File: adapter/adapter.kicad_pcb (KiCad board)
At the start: 2 copper layers, 93.6 x 71.8 mm, 44 parts, among them J10 Ribbon, J11 Ribbon, J12 Ribbon, J13 serial, J14 serial, J3 battery charge, J6 battery charge, J7 trackball, J8 trackball, J9 Ribbon, SW1 SW_SPST, SW2 SW_SPST, SW3 SW_SPDT, SW4 SW_SPDT, U1 eliteC, U2 eliteC

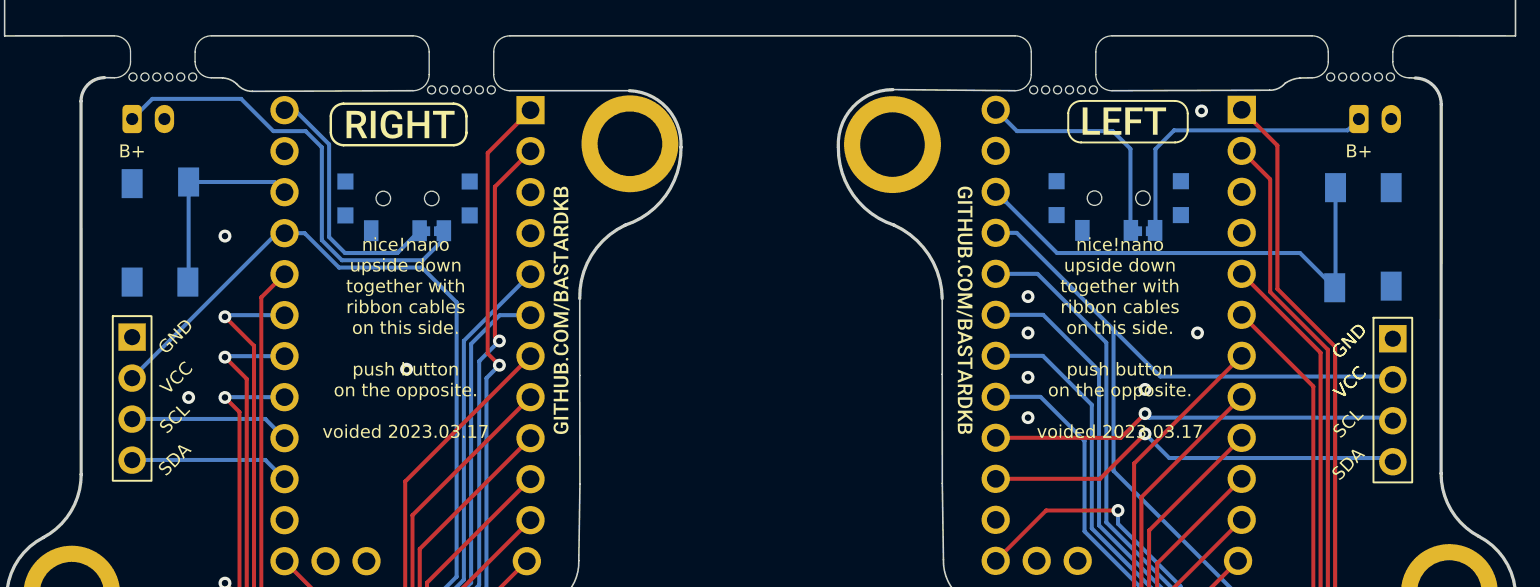
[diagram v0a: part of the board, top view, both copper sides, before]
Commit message: v0.2
removed serial ports
moved reset to be reachable
replace on/off switch to top and swapped to vertical through hole
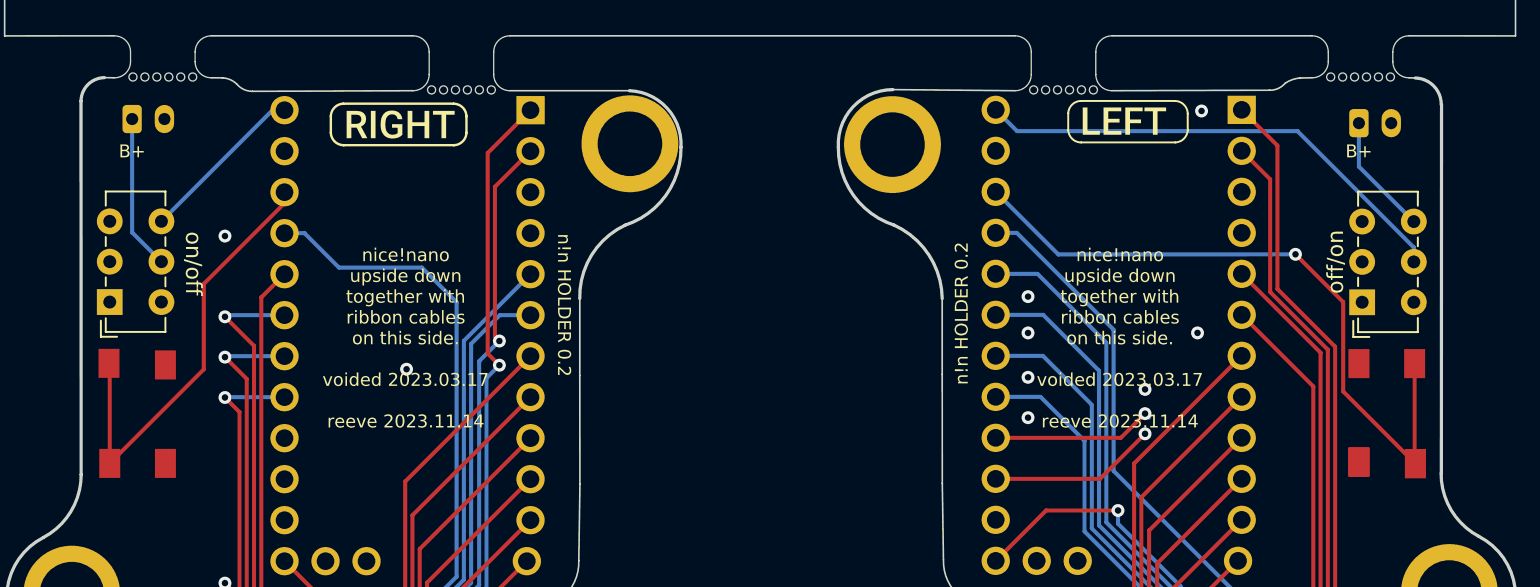
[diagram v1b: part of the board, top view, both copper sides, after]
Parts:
- removed J13, J14: serial, Library:PinHeader_1x04_P2.54mm_Vertical
- removed JP1, JP2: Jumper_2_Open, Library:power_switch_jumper
- removed SW3, SW4: SW_SPDT, Library:SW_SPDT+H-MSK12C01_hor(7pin_SMD)
- removed kibuzzard-61F01A92 (x2): G***, kibuzzard-61F01A92
- removed the kibuzzard-620B8593 at (133.5, 78.6)
- added ?: , , F.Cu at (196.0, 91.1)
- added ?: , , F.Cu at (192.5, 91.0)
- added REF**: SW3, Button_Switch_THT:SW_E-Switch_EG1271_SPDT, F.Cu at (115.1, 81.1)
- added off/on: SW_E-Switch_EG1271_SPDT, Button_Switch_THT:SW_E-Switch_EG1271_SPDT, F.Cu at (192.7, 81.1)
- SW1, SW2: moved to F.Cu
- moved SW1 11.3 mm to (116.9, 88.0)
- moved SW2 11.0 mm to (194.2, 88.0)
- moved J6 0.25 mm to (192.5, 70.0)
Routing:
- net +5V: track 115.5 -> 83.7 mm
- net bat_sw_l: track 28.4 -> 9.59 mm
- net sda_r: track 26.5 -> 10.4 mm
- net bat_r: track 14.4 -> 30.3 mm
- net scl_r: track 25.4 -> 10.2 mm
- net Rst: track 12.4 -> 27.6 mm
- net Rst2: track 29.7 -> 42.9 mm, vias 0 -> 1
- net bat_sw_r: track 18.4 -> 7.50 mm
- net scl_l: track 9.94 -> 0.00 mm
- net sda_l: track 9.94 -> 0.00 mm
- net bat_l: track 16.0 -> 11.1 mm
- net GND: vias 11 -> 10
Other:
- outline, holes or cut-outs redrawn
- board text added: "n!n HOLDER 0.2"
- board text added: "nice!nano upside down together with ribbon cables on this side. voided 2023.03.17 reeve 2023.11.14"
- board text added: "on/off"
- board text removed: "SCL"
- board text removed: "SDA"
- board text removed: "n!n HOLDER 0.1"
- board text removed: "nice!nano upside down together with ribbon cables on this side. push button on the opposite. voided 2023.03.17"

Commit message: Small fixes
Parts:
- removed kibuzzard-620B8593: G***, kibuzzard-620B8593
- moved J6 0.33 mm to (192.2, 70.0)
- moved J3 0.22 mm to (116.7, 69.8)
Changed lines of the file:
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@@
   )
   (footprint "Connector_JST:JST_PH_B2B-PH-K_1x02_P2.00mm_Vertical" (layer "F.Cu")
-    (at 192.5 70.004)
+    (at 192.175 70.002)
     (descr "JST PH series connector, B2B-PH-K (http://www.jst-mfg.com/product/pdf/eng/ePH.pdf), generated with kicad-footprint-generator")
     (tags "connector JST PH side entry")
@@
   )
   (footprint "Connector_JST:JST_PH_B2B-PH-K_1x02_P2.00mm_Vertical" (layer "F.Cu")
-    (at 116.5 69.75)
+    (at 116.725 69.75)
     (descr "JST PH series connector, B2B-PH-K (http://www.jst-mfg.com/product/pdf/eng/ePH.pdf), generated with kicad-footprint-generator")
     (tags "connector JST PH side entry")
@@
     )
   )
-  (footprint "kibuzzard-620B8593" (layer "B.Cu")
-    (at 177.5 78.6 180)
-    (descr "Converted using: scripting")
-    (tags "svg2mod")
-    (attr board_only exclude_from_pos_files exclude_from_bom)
-    (fp_text reference "kibuzzard-620B8593" (at 0 0.496912) (layer "B.SilkS") hide
-        (effects (font (size 0.000254 0.000254) (thickness 0.000003)) (justify mirror))
-    )
-    (fp_text value "G***" (at 0 -0.496912) (layer "B.SilkS") hide
-        (effects (font (size 0.000254 0.000254) (thickness 0.000003)) (justify mirror))
-    )
-    (fp_poly
-      (pts
-        (xy -0.393774 -0.496404)
-        (xy -0.512217 -0.496404)
-        (xy -0.15689 0.484001)
-        (xy -0.038447 0.484001)
-        (xy -0.393774 -0.496404)
-      )
-      (stroke (width 0) (type solid)) (fill solid) (layer "B.SilkS"))
-    (fp_poly
-      (pts
-        (xy -0.607095 -0.418889)
-        (xy -0.763984 -0.418889)
-        (xy -1.16644 0.221692)
-        (xy -1.16644 -0.418889)
-        (xy -1.32333 -0.418889)
-        (xy -1.32333 0.484001)
-        (xy -1.16644 0.484001)
-        (xy -0.762744 -0.15906)
-        (xy -0.762744 0.484001)
-        (xy -0.607095 0.484001)
-        (xy -0.607095 -0.418889)
-      )
-      (stroke (width 0) (type solid)) (fill solid) (layer "B.SilkS"))
-    (fp_poly
-      (pts
-        (xy 1.477739 -0.036277)
-        (xy 1.114351 -0.036277)
-        (xy 1.114351 -0.418889)
-        (xy 0.957461 -0.418889)
-        (xy 0.957461 0.484001)
-        (xy 1.531069 0.484001)
-        (xy 1.531069 0.357498)
-        (xy 1.114351 0.357498)
-        (xy 1.114351 0.088987)
-        (xy 1.477739 0.088987)
-        (xy 1.477739 -0.036277)
-      )
-      (stroke (width 0) (type solid)) (fill solid) (layer "B.SilkS"))
-    (fp_poly
-      (pts
-        (xy 2.175371 -0.036277)
-        (xy 1.811982 -0.036277)
-        (xy 1.811982 -0.418889)
-        (xy 1.655093 -0.418889)
-        (xy 1.655093 0.484001)
-        (xy 2.228701 0.484001)
-        (xy 2.228701 0.357498)
-        (xy 1.811982 0.357498)
-        (xy 1.811982 0.088987)
-        (xy 2.175371 0.088987)
-        (xy 2.175371 -0.036277)
-      )
-      (stroke (width 0) (type solid)) (fill solid) (layer "B.SilkS"))
-    (fp_poly
-      (pts
-        (xy -1.4796 0.008992)
-        (xy -1.636489 0.056121)
-        (xy -1.642794 0.14838)
-        (xy -1.661707 0.225068)
-        (xy -1.69323 0.286184)
-        (xy -1.76183 0.34618)
-        (xy -1.85415 0.366179)
-        (xy -1.944765 0.346258)
-        (xy -2.01321 0.286494)
-        (xy -2.045215 0.226033)
-        (xy -2.064749 0.150895)
-        (xy -2.071812 0.061082)
-        (xy -2.071812 0.008992)
-        (xy -2.065369 -0.082717)
-        (xy -2.046042 -0.159405)
-        (xy -2.013831 -0.221072)
-        (xy -1.94461 -0.281998)
-        (xy -1.85291 -0.302307)
-        (xy -1.760745 -0.282463)
-        (xy -1.69261 -0.222932)
-        (xy -1.661432 -0.161885)
-        (xy -1.642725 -0.084577)
-        (xy -1.636489 0.008992)
-        (xy -1.636489 0.056121)
-        (xy -1.4796 0.008992)
-        (xy -1.484698 -0.075861)
-        (xy -1.499995 -0.153479)
-        (xy -1.525488 -0.223862)
-        (xy -1.581221 -0.312384)
-        (xy -1.656643 -0.377651)
-        (xy -1.716347 -0.407451)
-        (xy -1.781769 -0.425331)
-        (xy -1.85291 -0.431292)
-        (xy -1.956702 -0.417881)
-        (xy -2.048557 -0.377651)
-        (xy -2.124677 -0.312617)
-        (xy -2.181262 -0.224792)
-        (xy -2.207342 -0.15527)
-        (xy -2.223155 -0.078996)
-        (xy -2.228701 0.004031)
-        (xy -2.228701 0.05488)
-        (xy -2.223499 0.139492)
-        (xy -2.207893 0.217213)
-        (xy -2.181882 0.288044)
-        (xy -2.146398 0.35016)
-        (xy -2.10237 0.401733)
-        (xy -2.049797 0.442764)
-        (xy -1.958253 0.482994)
-        (xy -1.85415 0.496404)
-        (xy -1.750048 0.483149)
-        (xy -1.658503 0.443384)
-        (xy -1.582927 0.378737)
-        (xy -1.526729 0.290835)
-        (xy -1.500821 0.220865)
-        (xy -1.485112 0.14366)
-        (xy -1.4796 0.059221)
-        (xy -1.4796 0.008992)
-      )
-      (stroke (width 0) (type solid)) (fill solid) (layer "B.SilkS"))
-    (fp_poly
-      (pts
-        (xy 0.801191 0.008992)
-        (xy 0.644302 0.056121)
-        (xy 0.637997 0.14838)
-        (xy 0.619084 0.225068)
-        (xy 0.587561 0.286184)
-        (xy 0.518961 0.34618)
-        (xy 0.426641 0.366179)
-        (xy 0.336026 0.346258)
-        (xy 0.267581 0.286494)
-        (xy 0.235576 0.226033)
-        (xy 0.216042 0.150895)
-        (xy 0.208979 0.061082)
-        (xy 0.208979 0.008992)
-        (xy 0.215422 -0.082717)
-        (xy 0.234749 -0.159405)
-        (xy 0.26696 -0.221072)
-        (xy 0.336181 -0.281998)
-        (xy 0.427881 -0.302307)
-        (xy 0.520046 -0.282463)
-        (xy 0.588181 -0.222932)
-        (xy 0.619359 -0.161885)
-        (xy 0.638066 -0.084577)
-        (xy 0.644302 0.008992)
-        (xy 0.644302 0.056121)
-        (xy 0.801191 0.008992)
-        (xy 0.796093 -0.075861)
-        (xy 0.780796 -0.153479)
-        (xy 0.755303 -0.223862)
-        (xy 0.69957 -0.312384)
-        (xy 0.624148 -0.377651)
-        (xy 0.564444 -0.407451)
-        (xy 0.499022 -0.425331)
-        (xy 0.427881 -0.431292)
-        (xy 0.324089 -0.417881)
-        (xy 0.232234 -0.377651)
-        (xy 0.156115 -0.312617)
-        (xy 0.099529 -0.224792)
-        (xy 0.073449 -0.15527)
-        (xy 0.057636 -0.078996)
-        (xy 0.05209 0.004031)
-        (xy 0.05209 0.05488)
-        (xy 0.057292 0.139492)
-        (xy 0.072898 0.217213)
-        (xy 0.098909 0.288044)
-        (xy 0.134393 0.35016)
-        (xy 0.178421 0.401733)
-        (xy 0.230994 0.442764)
-        (xy 0.322538 0.482994)
-        (xy 0.426641 0.496404)
-        (xy 0.530743 0.483149)
-        (xy 0.622288 0.443384)
-        (xy 0.697864 0.378737)
-        (xy 0.754063 0.290835)
-        (xy 0.77997 0.220865)
-        (xy 0.795679 0.14366)
-        (xy 0.801191 0.059221)
-        (xy 0.801191 0.008992)
-      )
-      (stroke (width 0) (type solid)) (fill solid) (layer "B.SilkS"))
-  )
   (footprint "kibuzzard-6208EFFE" (layer "B.Cu")
     (at 177.972311 70.078921 180)
@@
     (effects (font (size 0.8 0.8) (thickness 0.15)) (justify mirror))
   )
-  (gr_text "B+" (at 192.5 71.75) (layer "B.SilkS")
+  (gr_text "B+" (at 192.175 71.748) (layer "B.SilkS")
     (effects (font (size 0.8 0.8) (thickness 0.15)) (justify mirror))
   )
@@
     (effects (font (size 0.8 0.8) (thickness 0.15)) (justify mirror))
   )
-  (gr_text "B+" (at 116.5 71.75) (layer "B.SilkS")
+  (gr_text "B+" (at 116.725 71.75) (layer "B.SilkS")
     (effects (font (size 0.8 0.8) (thickness 0.15)) (justify mirror))
   )
@@
     (effects (font (size 0.8 0.8) (thickness 0.15)))
   )
-  (gr_text "B+" (at 116.5 71.75) (layer "F.SilkS")
+  (gr_text "B+" (at 116.725 71.75) (layer "F.SilkS")
     (effects (font (size 0.8 0.8) (thickness 0.15)))
   )
@@
     (effects (font (size 0.8 0.8) (thickness 0.15)))
   )
-  (gr_text "B+" (at 192.5 71.75) (layer "F.SilkS")
+  (gr_text "B+" (at 192.175 71.748) (layer "F.SilkS")
     (effects (font (size 0.8 0.8) (thickness 0.15)))
   )
@@
   (segment (start 126.586396 69.2) (end 125.94 69.2) (width 0.25) (layer "B.Cu") (net 39))
   (segment (start 125.2004 69.2) (end 125.94 69.2) (width 0.25) (layer "B.Cu") (net 39))
-  (segment (start 195.9 78.6) (end 195.9 77.7) (width 0.25) (layer "B.Cu") (net 40))
-  (segment (start 188.7 70.5) (end 171.32 70.5) (width 0.25) (layer "B.Cu") (net 40))
+  (segment (start 189.35 70.5) (end 171.32 70.5) (width 0.25) (layer "B.Cu") (net 40))
+  (segment (start 194.3 77) (end 194.3 75.45) (width 0.25) (layer "B.Cu") (net 40))
+  (segment (start 195.9 78.6) (end 194.3 77) (width 0.25) (layer "B.Cu") (net 40))
   (segment (start 171.32 70.5) (end 170 69.18) (width 0.25) (layer "B.Cu") (net 40))
-  (segment (start 195.9 77.7) (end 188.7 70.5) (width 0.25) (layer "B.Cu") (net 40))
-  (segment (start 116.5 76.7748) (end 116.5 69.75) (width 0.25) (layer "B.Cu") (net 41))
-  (segment (start 118.3128 78.5876) (end 116.5 76.7748) (width 0.25) (layer "B.Cu") (net 41))
-  (segment (start 192.5 70.004) (end 192.5 72.7) (width 0.25) (layer "B.Cu") (net 42))
-  (segment (start 192.5 72.7) (end 195.9 76.1) (width 0.25) (layer "B.Cu") (net 42))
+  (segment (start 194.3 75.45) (end 189.35 70.5) (width 0.25) (layer "B.Cu") (net 40))
+  (segment (start 116.725 76.9998) (end 116.725 69.75) (width 0.25) (layer "F.Cu") (net 41))
+  (segment (start 118.3128 78.5876) (end 116.725 76.9998) (width 0.25) (layer "F.Cu") (net 41))
+  (segment (start 195.9 76.1) (end 192.2 72.4) (width 0.25) (layer "F.Cu") (net 42))
+  (segment (start 192.2 70.027) (end 192.175 70.002) (width 0.25) (layer "F.Cu") (net 42))
+  (segment (start 192.2 72.4) (end 192.2 70.027) (width 0.25) (layer "F.Cu") (net 42))
   (zone (net 27) (net_name "GND") (layers "F&B.Cu") (hatch edge 0.5)
     (connect_pads (clearance 0.508))
